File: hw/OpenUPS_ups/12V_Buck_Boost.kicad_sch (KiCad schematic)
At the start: 61 parts, among them Q701 Q_NMOS_GDS, Q702 Q_NMOS_GDS, Q705 Q_NMOS_GDS, Q706 Q_NMOS_GDS, U702 NCP81599

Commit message: More cleanups and stuff
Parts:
- gave numbers to parts that had none: 6
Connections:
- net Vout: now also R717.2, R718.2, R723.2
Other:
- moved on the sheet: C501, C706, C708, C709, C710, C711, C712, C713, C714, C715, C716, C717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

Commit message: Work on Buck Boosts
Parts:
- C701, C702: value 1n -> 10n
- R706, R707, R708, R709: value ? -> 10k
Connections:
- net EN: now also R708.2, R709.1, U702.16 (EN); no longer R709.2
- new net +3.3VA: R709.2
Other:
- note added: "Current Sense analog outputs High impedance load only Place RC near ADC input (that's a current output) 2.54V max RC > 100/(2*pi*f_sw) With Rsense = 5mOhm: R = 10k -> Vcs = 2V/10A * I_sense Assuming 300kHz operation: C > 100/(10k*2*pi*300k) -> C > 5.3n"
- note added: "EN is complicated: ~ 0.8V - I2C and LDO ON ~ 2.15V - Switching ON Also sources 3uA (negligible). When schematic port "EN" floats, IC is on but not switching. Pulling either HI or LO, chip may be enabled or reset."
- note removed: "Current Sense analog outputs High impedance load only"
- note removed: "EN is complicated: ~ 0.8V - I2C and LDO ON ~ 2.15V - Switching ON Sources 3uA Abs Max 5.5V"
- moved on the sheet: C501, C502, C503, C701, C702, C703, C704, C705, C706, C708, C709, C710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

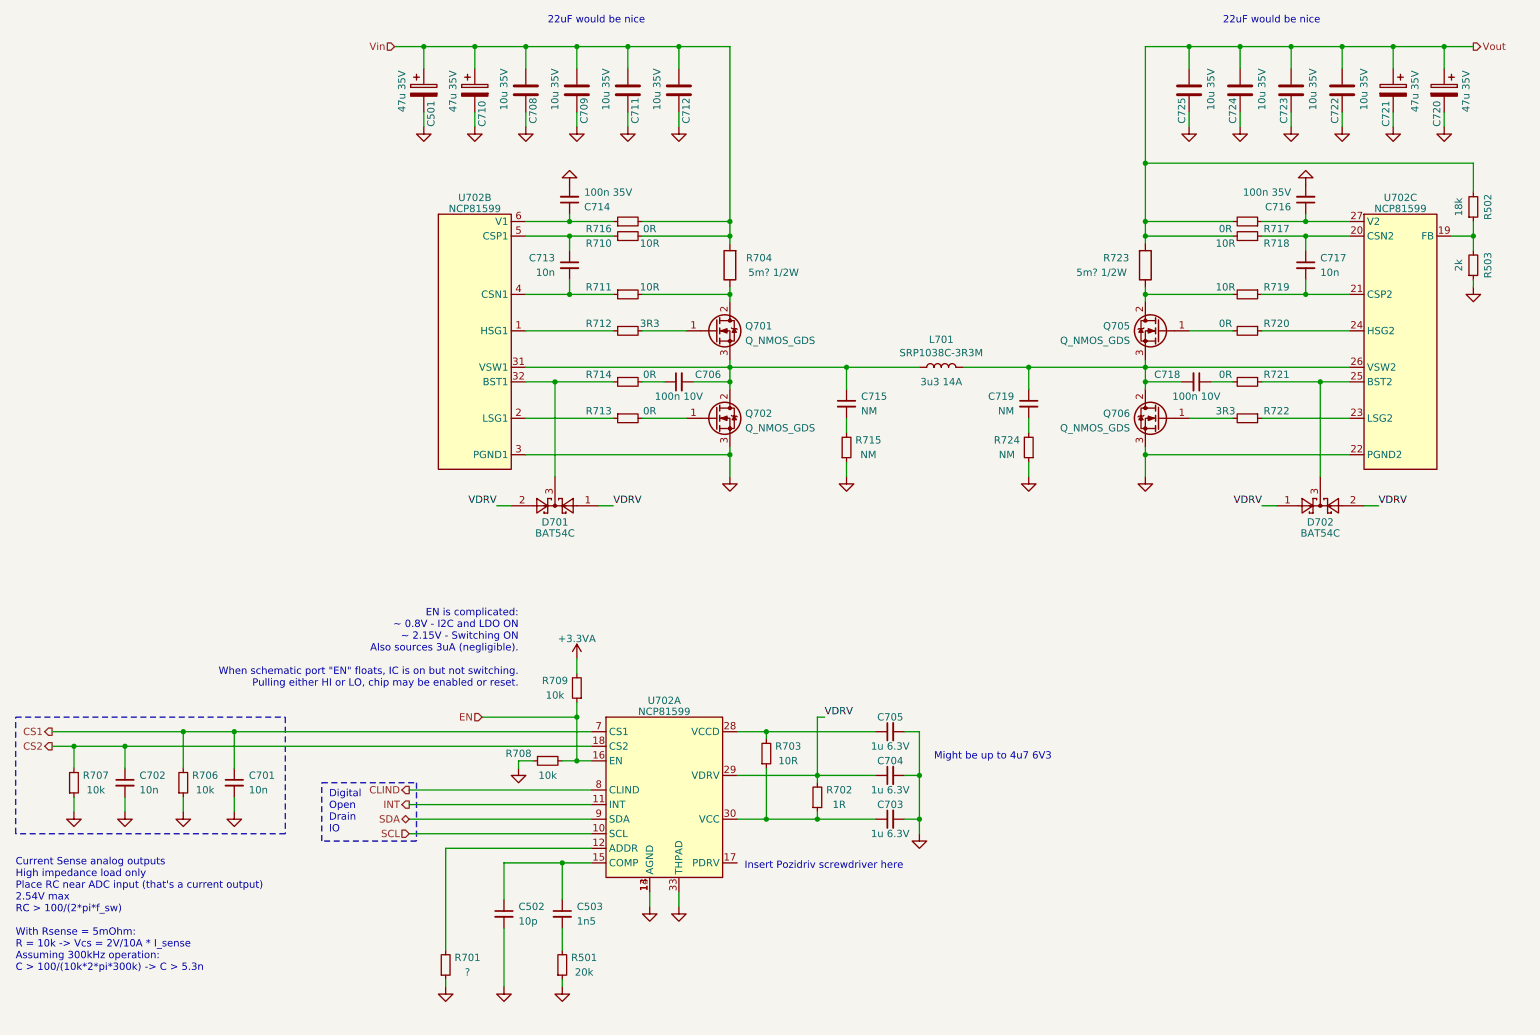
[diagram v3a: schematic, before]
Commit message: Preliminary NMOS: AON7534; USB-C selected.
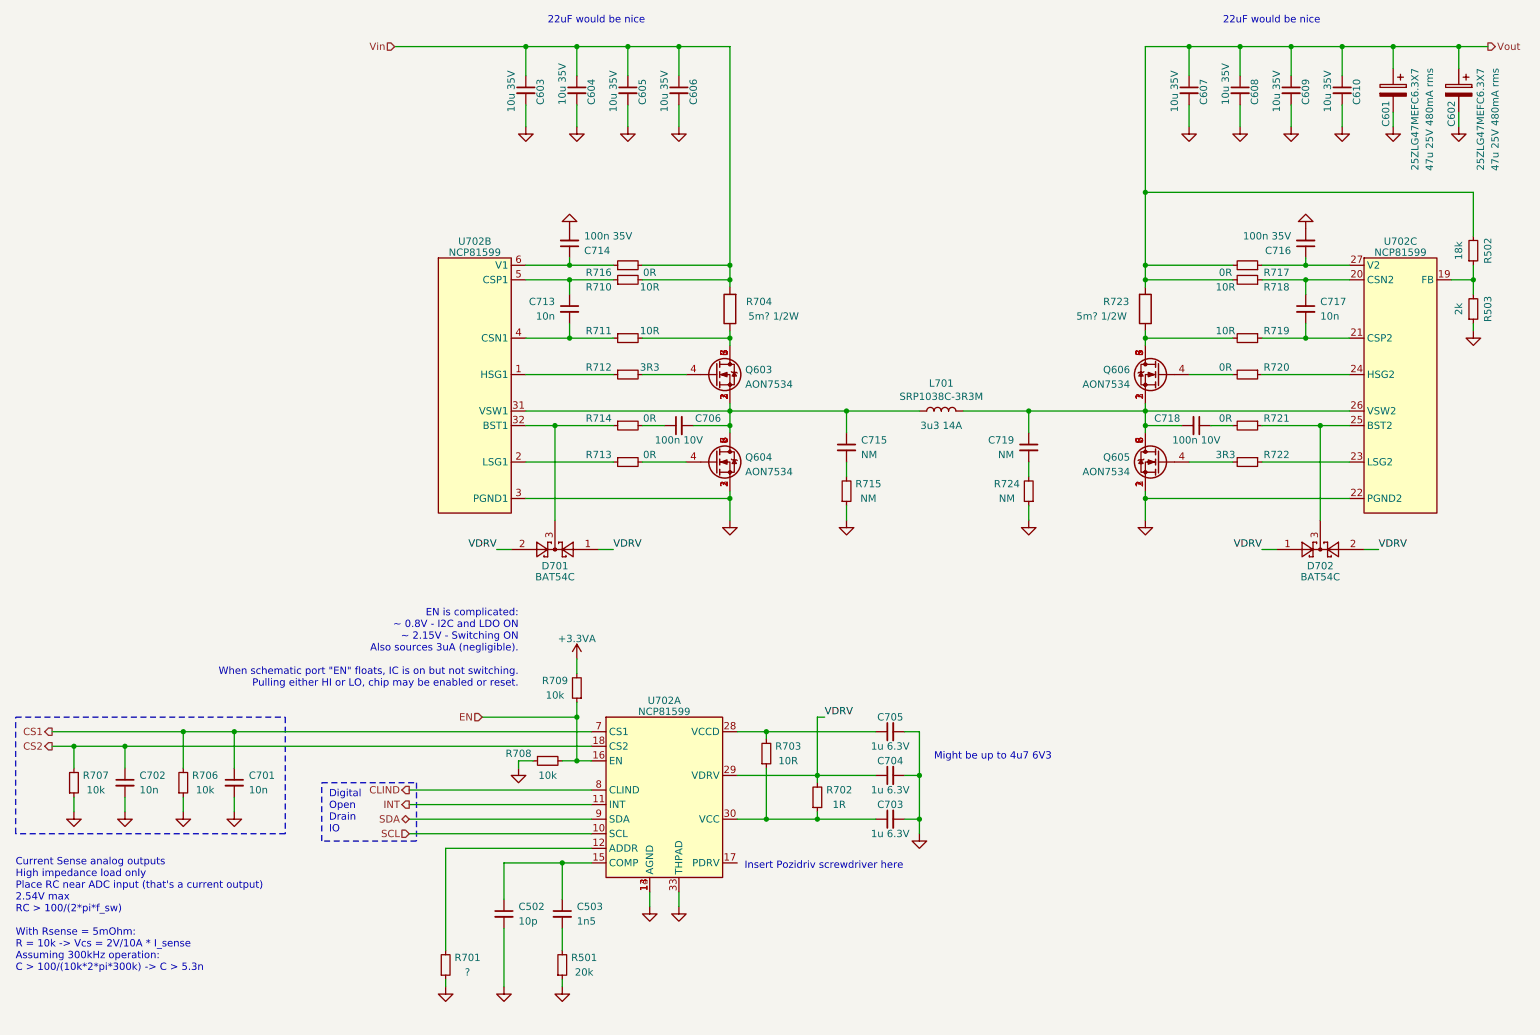
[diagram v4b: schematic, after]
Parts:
- removed C501, C710, C720, C721: 47u 35V, Capacitor_SMD:CP_Elec_6.3x7.7, symbol Device:C_Polarized
- removed C708, C709, C711, C712, C722, C723, C724, C725: 10u 35V, Capacitor_SMD:C_1206_3216Metric, symbol Device:C
- removed Q701, Q702, Q705, Q706: Q_NMOS_GDS, Package_TO_SOT_SMD:TO-263-2, symbol Device:Q_NMOS_GDS
- added C601, C602: 25ZLG47MEFC6.3X7, Capacitor_THT:CP_Radial_D6.3mm_P2.50mm, symbol Device:C_Polarized
- added C603, C604, C605, C606, C607, C608, C609, C610: 10u 35V, Capacitor_SMD:C_0603_1608Metric, symbol Device:C_Small
- added Q603, Q604, Q605, Q606: AON7534, footprints:DFN 3x3 MOSFET, symbol Device:Q_NMOS_GDS
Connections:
- net GND: now also C601.2, C602.2, C603.2, C604.2, C605.2, C606.2, C607.2, C608.2, C609.2, C610.2, Q604.1 (S), Q604.2 (S), Q604.3 (S), Q605.1 (S), Q605.2 (S), Q605.3 (S)
- net Vin: now also C603.1, C604.1, C605.1, C606.1
- net Vout: now also C601.1, C602.1, C607.1, C608.1, C609.1, C610.1
- net at C718.2, C719.1, L701.2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: now also Q605.5 (D), Q605.6 (D), Q605.7 (D), Q605.8 (D), Q606.1 (S), Q606.2 (S), Q606.3 (S)
- net at R719.2, R723.1: now also Q606.5 (D), Q606.6 (D), Q606.7 (D), Q606.8 (D)
- net at R704.1, R711.2: now also Q603.5 (D), Q603.6 (D), Q603.7 (D), Q603.8 (D)
- net at C706.2, C715.1, L701.1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: now also Q603.1 (S), Q603.2 (S), Q603.3 (S), Q604.5 (D), Q604.6 (D), Q604.7 (D), Q604.8 (D)
- net at R712.2: now also Q603.4 (G)
- net at R720.2: now also Q606.4 (G)
- net at R713.2: now also Q604.4 (G)
- net at R722.2: now also Q605.4 (G)
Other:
- moved on the sheet: C706, C713, C714, C715, C716, C717, C718, C719, D701, D702, L701, R502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

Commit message: Initial placement effort
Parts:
- renumbered C702 to C601, C701 to C602, C502 to C603, C603 to C604, C503 to C605, C714 to C606, C713 to C607, C604 to C608, C605 to C609, C606 to C610, C706 to C611, C715 to C612, C705 to C613, C704 to C614, C703 to C615, C719 to C616, C607 to C617, C718 to C618, C608 to C619, C609 to C620, C716 to C621, C717 to C622, C610 to C623, C601 to C624, C602 to C625, D701 to D601, D702 to D602, L701 to L601, Q603 to Q601, Q604 to Q602, Q606 to Q603, Q605 to Q604, R707 to R601, R706 to R602, R701 to R603, R708 to R604, R501 to R605, R709 to R606, R716 to R607, R710 to R608, R711 to R609, R712 to R610, R714 to R611, R713 to R612, R704 to R613, R703 to R614, R702 to R615, R715 to R616, R724 to R617, R723 to R618, R717 to R619, R718 to R620, R719 to R621, R720 to R622, R721 to R623, R722 to R624, R502 to R625, R503 to R626, U702 to U601

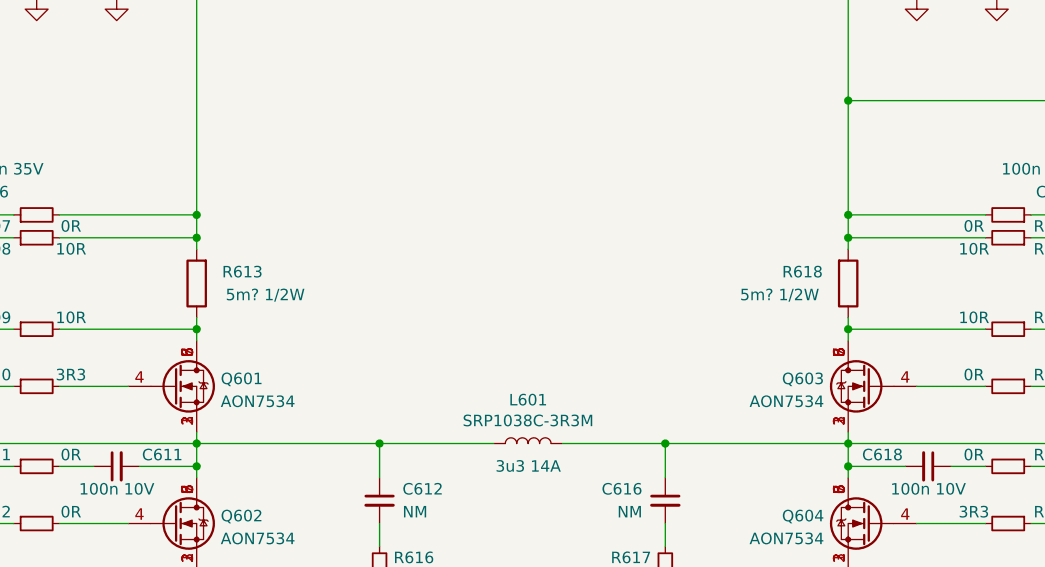
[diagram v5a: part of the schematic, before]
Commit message: Unified sense resistors to 10mR; Placement
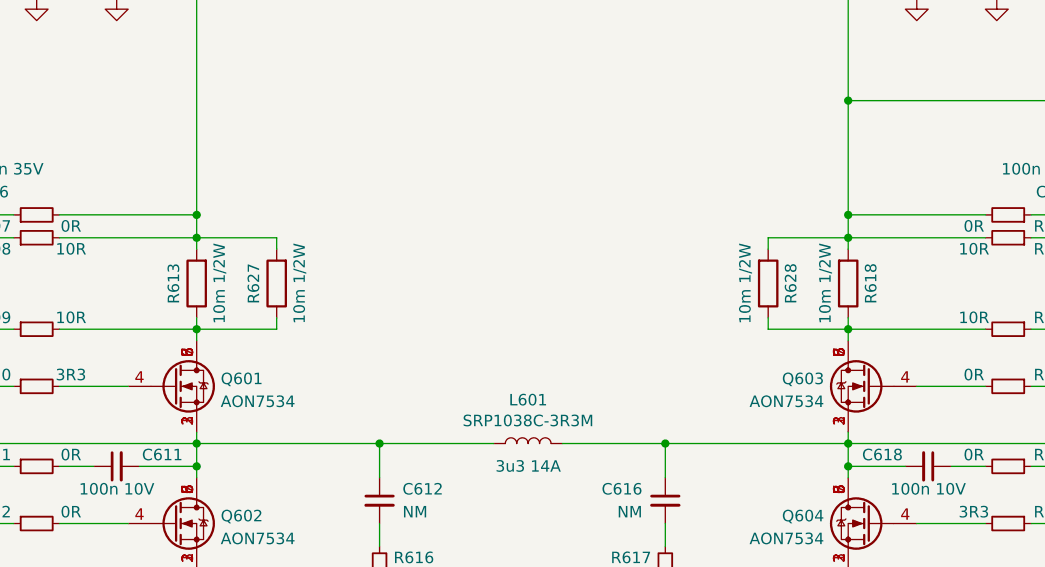
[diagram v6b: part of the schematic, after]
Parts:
- added R627, R628: 10m 1/2W, Resistor_SMD:R_1206_3216Metric, symbol Device:R
- R613, R618: value 5m? 1/2W -> 10m 1/2W; footprint Resistor_SMD:R_2512_6332Metric -> Resistor_SMD:R_1206_3216Metric
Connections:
- net Vin: now also R627.2
- net Vout: now also R628.2
- net at Q603.5 (D), Q603.6 (D), Q603.7 (D)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: now also R628.1
- net at Q601.5 (D), Q601.6 (D), Q601.7 (D)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: now also R627.1
